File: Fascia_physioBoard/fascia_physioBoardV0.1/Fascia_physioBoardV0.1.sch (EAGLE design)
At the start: 89 parts, among them CN2 CA0612KRX7R9BB102, CN3 CA0612KRX7R9BB102, CN4 CA0612KRX7R9BB102, CN5 CA0612KRX7R9BB102, CN6 CA0612KRX7R9BB102, J1 MOLEX_52437-2471MOLEX_52437-2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, J2 MOLEX_52437-2471MOLEX_52437-2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, J3 MOLEX_51296-1294MOLEX_51296-1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, U1 ADS1299-X, U10 TPD4E1B06DCKR, U11 TPD4E1B06DCKR, U12 OPA320AIDBVRDBV5-L, U13 ADUM5028, U2 OPA2320AIDGKT_NOVA8-SOIC-L, U3 OPA2320AIDGKT_NOVAL8-SOIC-L, U4 HCNR200-300E, U5 OPA320AIDBVRDBV5-L, U6 TPD4E1B06DCKR, U7 TPD4E1B06DCKR, U8 TPD4E1B06DCKR, U9 TPD4E1B06DCKR

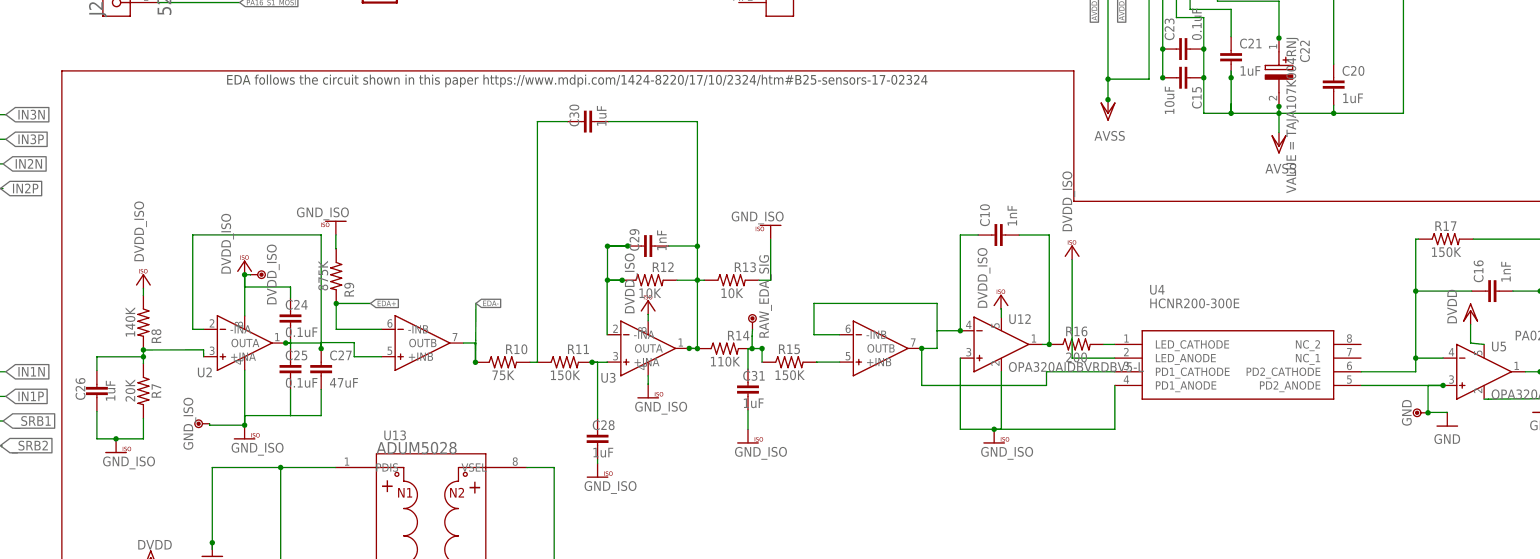
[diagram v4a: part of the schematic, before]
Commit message: made changes to eda schematic and board files. fixing the issues preventing the V0 to work correctly
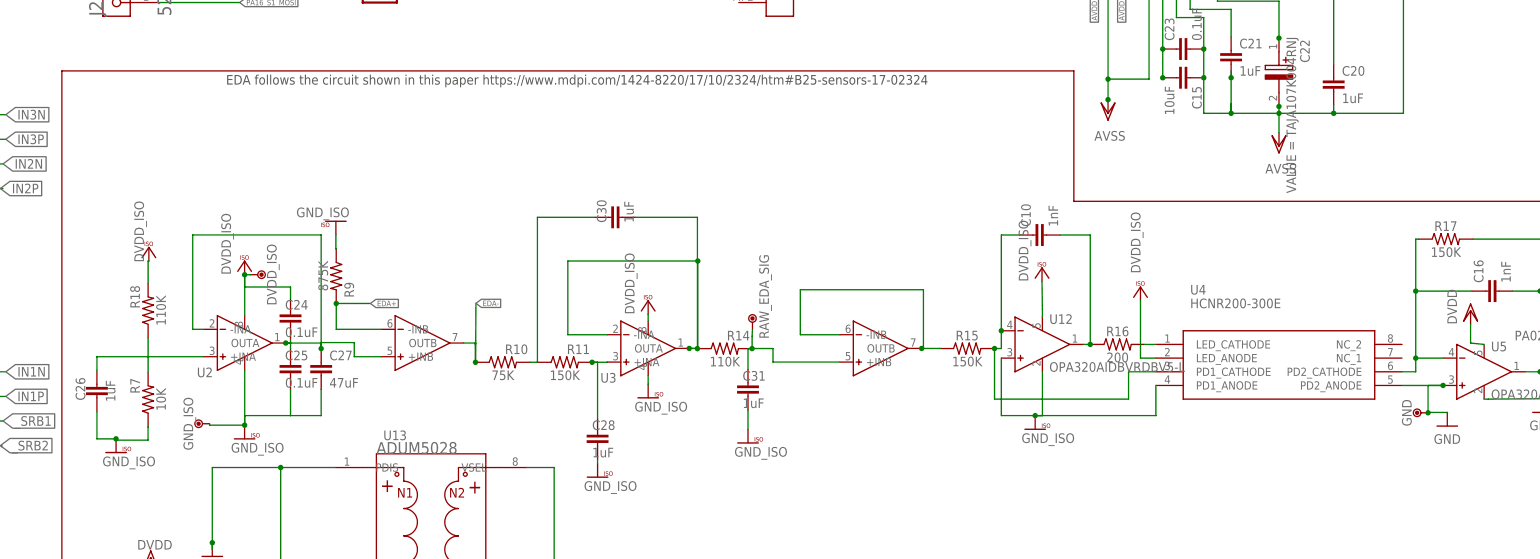
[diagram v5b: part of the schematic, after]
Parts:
- removed C29: 1nF, novaXR:1NF-0402T-16V-10%
- removed R12, R13: 10K, novaXR:10K
- removed R8: 140K, novaXR:140K
- added R18: 110K, novaXR:110K
- R7: value 20K -> 10K; device novaXR:20K -> novaXR:10K
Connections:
- removed net N$14: R15.2, U3.+INB
- removed net N$15: C10.1, U12.IN-, U3.-INB, U3.OUTB, U4.PD1_CATHODE
- new net N$12: C26.1, R18.1, R7.2, U2.+INA
- net DVDD_ISO: now also R18.2; no longer R8.1
- net GND_ISO: now also R7.1; no longer R13.2, R7.2
- net N$10: now also R15.1, U3.-INB, U3.OUTB; no longer C29.1, R12.1, U3.-INA
- net N$11: now also U3.-INA; no longer C29.2, R12.2, R13.1
- net N$2: now also C10.1, R15.2, U12.IN-, U4.PD1_CATHODE; no longer C26.1, R7.1, R8.2, U2.+INA
- net N$4: now also U3.+INB; no longer R15.1
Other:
- moved on the sheet: C10, C30, R15, R16, R7, U12, U4

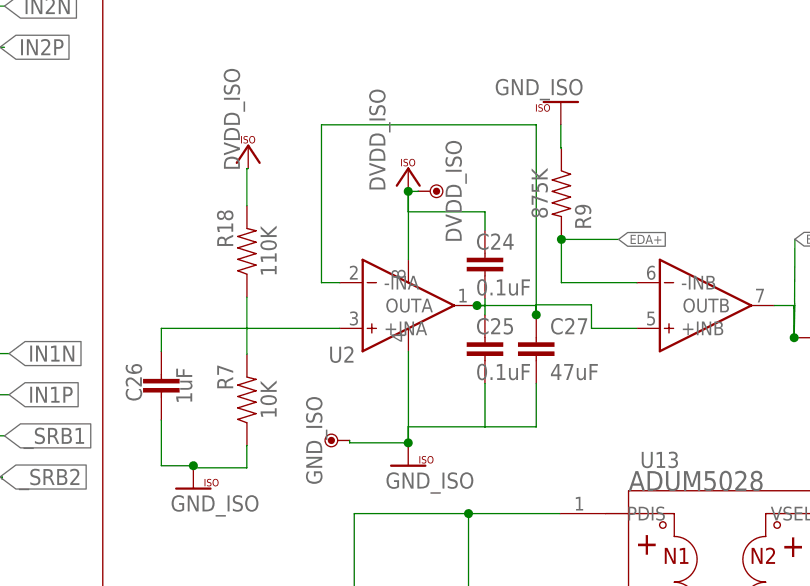
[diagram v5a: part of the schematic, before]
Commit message: changed values used on the board to be reflected on the schematic
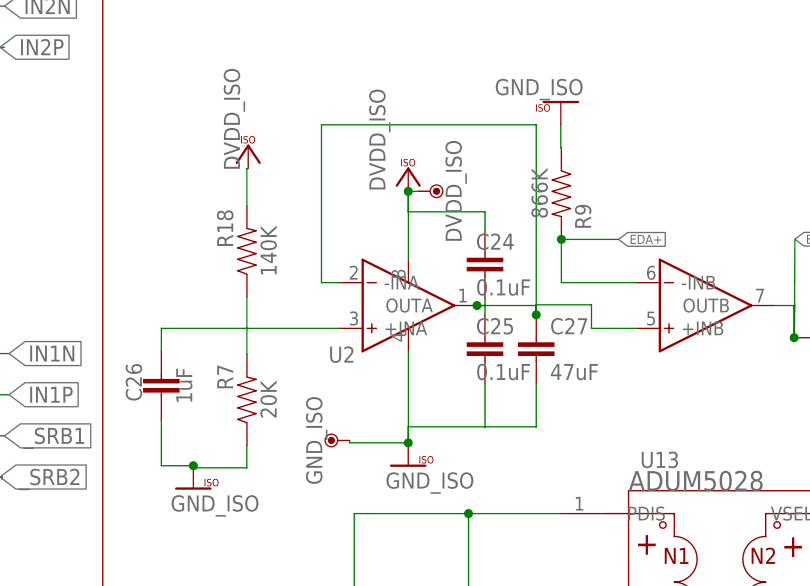
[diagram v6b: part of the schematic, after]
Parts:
- R18: value 110K -> 140K
- R7: value 10K -> 20K
- R9: value 875K -> 866K
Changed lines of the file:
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@@
 <?xml version="1.0" encoding="utf-8"?>
 <!DOCTYPE eagle SYSTEM "eagle.dtd">
-<eagle version="9.5.1">
+<eagle version="9.6.0">
 <drawing>
 <settings>
@@
 <part name="U$31" library="supply1" deviceset="GND_ISO" device=""/>
 <part name="U$19" library="supply1" deviceset="DVDD_ISO" device=""/>
-<part name="R9" library="novaXR" deviceset="875K" device="" value="875K"/>
+<part name="R9" library="novaXR" deviceset="875K" device="" value="866K"/>
 <part name="R10" library="novaXR" deviceset="75K" device="" value="75K"/>
 <part name="R11" library="novaXR" deviceset="150K" device="" value="150K"/>
@@
 <part name="J3" library="Molex - 51296-1294" deviceset="MOLEX_51296-1294" device="MOLEX_51296-1294_0_0"/>
 <part name="J4" library="SparkFun-Connectors" library_urn="urn:adsk.eagle:library:513" deviceset="CONN_02" device="" package3d_urn="urn:adsk.eagle:package:38039/1"/>
-<part name="R7" library="novaXR" deviceset="10K" device="" value="10K"/>
-<part name="R18" library="novaXR" deviceset="110K" device="" value="110K"/>
+<part name="R7" library="novaXR" deviceset="10K" device="" value="20K"/>
+<part name="R18" library="novaXR" deviceset="110K" device="" value="140K"/>
 </parts>
 <sheets>
